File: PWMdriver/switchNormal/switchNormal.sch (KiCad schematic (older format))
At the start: 6 parts

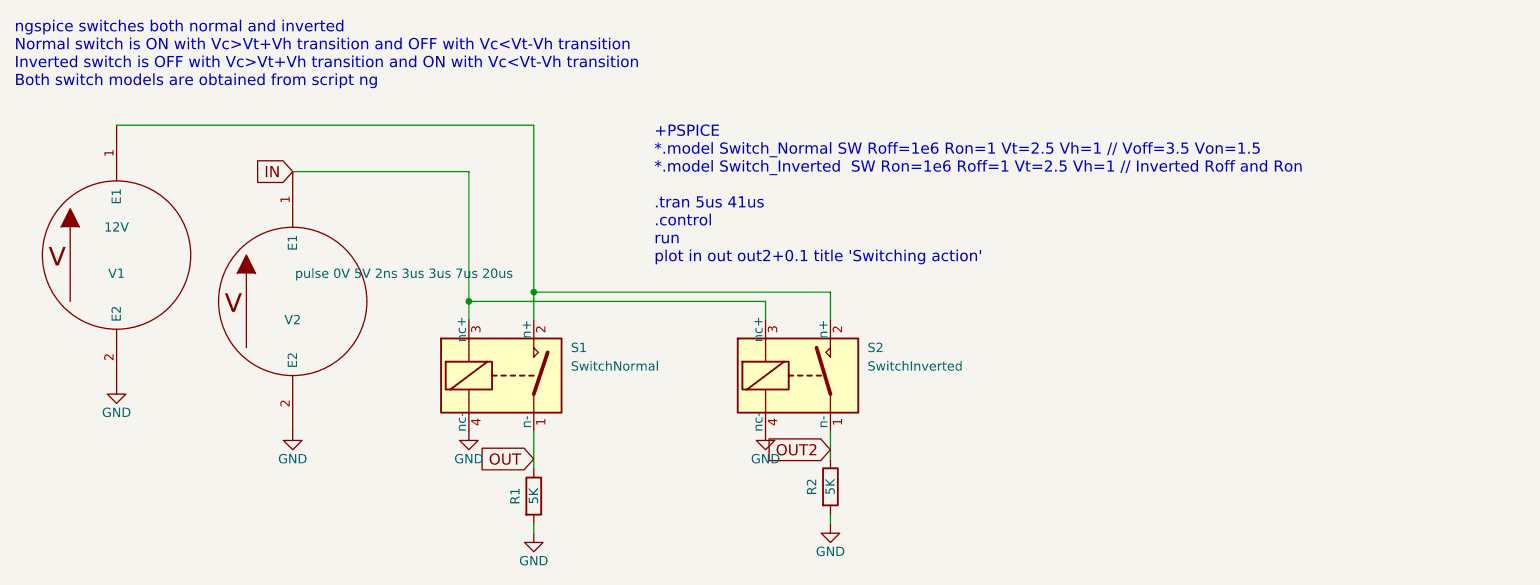
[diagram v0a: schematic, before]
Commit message: updated switches to NO and NC
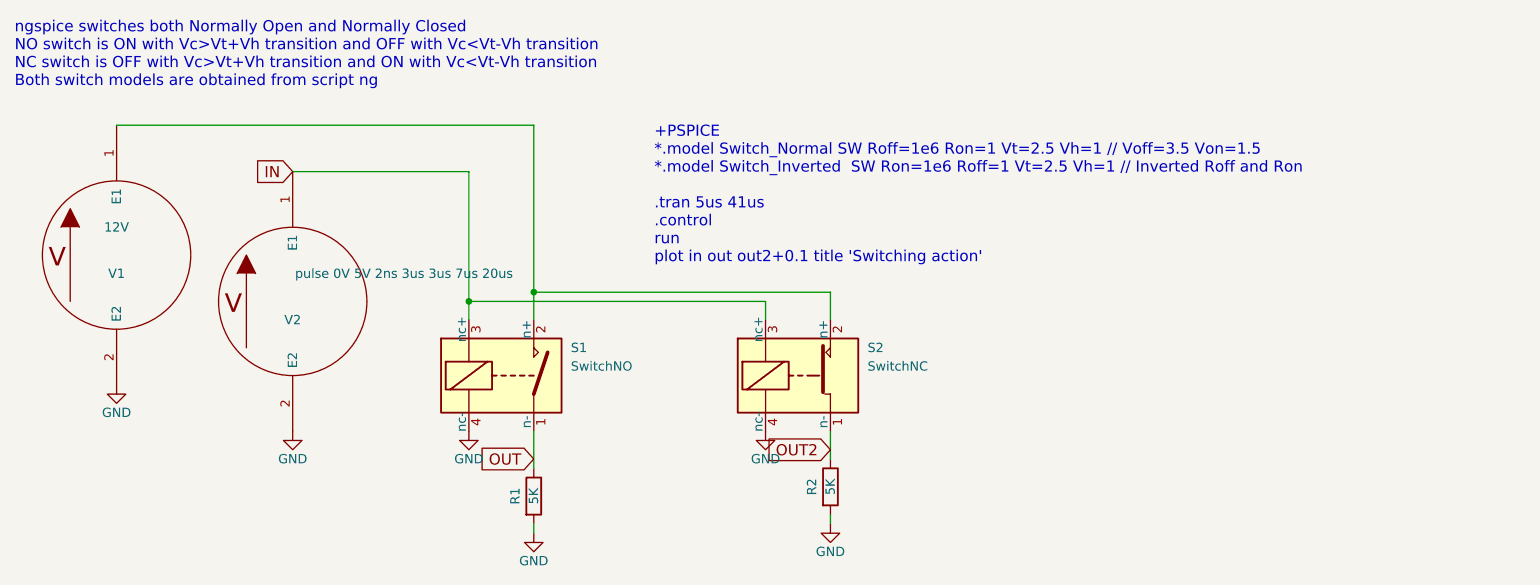
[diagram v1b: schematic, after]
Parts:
- removed S1: SwitchNormal, switchSpice, symbol SwitchNormal
- removed S2: SwitchInverted, switchSpice, symbol SwitchInverted
- added S1: SwitchNO, switchSpice, symbol SwitchNO
- added S2: SwitchNC, switchSpice, symbol SwitchNC
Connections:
- net GND: now also S1.4 (nc-), S2.4 (nc-)
- net IN: now also S1.3 (nc+), S2.3 (nc+)
- net OUT: now also S1.1 (n-)
- net OUT2: now also S2.1 (n-)
- net at V1.1 (E1): now also S1.2 (n+), S2.2 (n+)
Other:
- note added: "ngspice switches both Normally Open and Normally Closed\nNO switch is ON with Vc>Vt+Vh transition and OFF with Vc<Vt-Vh transition\nNC switch is OFF with Vc>Vt+Vh transition and ON with Vc<Vt-Vh transition\nBoth switch models are obtained from script ng"
- note removed: "ngspice switches both normal and inverted\nNormal switch is ON with Vc>Vt+Vh transition and OFF with Vc<Vt-Vh transition\nInverted switch is OFF with Vc>Vt+Vh transition and ON with Vc<Vt-Vh transition\nBoth switch models are obtained from script ng"
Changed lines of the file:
@@
 $EndDescr
 $Comp
-L GND #PWR01
+L GND #PWR3
 U 1 1 5B0C8932
 P 3650 2800
-F 0 "#PWR01" H 3650 2550 50  0001 C CNN
+F 0 "#PWR3" H 3650 2550 50  0001 C CNN
 F 1 "GND" H 3650 2650 50  0000 C CNN
 F 2 "" H 3650 2800 50  0001 C CNN
@@
 $EndComp
 $Comp
-L GND #PWR02
+L GND #PWR2
 U 1 1 5B0C8934
 P 2700 2800
-F 0 "#PWR02" H 2700 2550 50  0001 C CNN
+F 0 "#PWR2" H 2700 2550 50  0001 C CNN
 F 1 "GND" H 2700 2650 50  0000 C CNN
 F 2 "" H 2700 2800 50  0001 C CNN
@@
 	4000 3300 4000 3350
 $Comp
-L GND #PWR03
+L GND #PWR6
 U 1 1 5B0C8935
 P 4000 3350
-F 0 "#PWR03" H 4000 3100 50  0001 C CNN
+F 0 "#PWR6" H 4000 3100 50  0001 C CNN
 F 1 "GND" H 4000 3200 50  0000 C CNN
 F 2 "" H 4000 3350 50  0001 C CNN
@@
 $EndComp
 $Comp
-L GND #PWR04
+L GND #PWR1
 U 1 1 5B0C893B
 P 1750 2550
-F 0 "#PWR04" H 1750 2300 50  0001 C CNN
+F 0 "#PWR1" H 1750 2300 50  0001 C CNN
 F 1 "GND" H 1750 2400 50  0000 C CNN
 F 2 "" H 1750 2550 50  0001 C CNN
@@
 	4000 1150 1750 1150
 $Comp
-L GND #PWR05
+L GND #PWR4
 U 1 1 5B0D0161
 P 5250 2800
-F 0 "#PWR05" H 5250 2550 50  0001 C CNN
+F 0 "#PWR4" H 5250 2550 50  0001 C CNN
 F 1 "GND" H 5250 2650 50  0000 C CNN
 F 2 "" H 5250 2800 50  0001 C CNN
@@
 	5600 3250 5600 3300
 $Comp
-L GND #PWR06
+L GND #PWR5
 U 1 1 5B0D0169
 P 5600 3300
-F 0 "#PWR06" H 5600 3050 50  0001 C CNN
+F 0 "#PWR5" H 5600 3050 50  0001 C CNN
 F 1 "GND" H 5600 3150 50  0000 C CNN
 F 2 "" H 5600 3300 50  0001 C CNN
@@
 	5250 2100 3650 2100
 Text Notes 1200 950  0    60   ~ 0
-ngspice switches both normal and inverted\nNormal switch is ON with Vc>Vt+Vh transition and OFF with Vc<Vt-Vh transition\nInverted switch is OFF with Vc>Vt+Vh transition and ON with Vc<Vt-Vh transition\nBoth switch models are obtained from script ng
-$Comp
-L SwitchNormal S1
-U 1 1 5B0E5BFC
-P 3850 2500
-F 0 "S1" H 4200 2650 50  0000 L CNN
-F 1 "SwitchNormal" H 4200 2550 50  0000 L CNN
-F 2 "switchSpice" H 5120 2470 50  0001 C CNN
-F 3 "" H 3850 2500 50  0001 C CNN
-	1    3850 2500
-	1    0    0    -1
-$EndComp
-$Comp
-L SwitchInverted S2
-U 1 1 5B0E5CAD
-P 5450 2500
-F 0 "S2" H 5800 2650 50  0000 L CNN
-F 1 "SwitchInverted" H 5800 2550 50  0000 L CNN
-F 2 "switchSpice" H 6720 2470 50  0001 C CNN
-F 3 "" H 5450 2500 50  0001 C CNN
-	1    5450 2500
-	1    0    0    -1
-$EndComp
+ngspice switches both Normally Open and Normally Closed\nNO switch is ON with Vc>Vt+Vh transition and OFF with Vc<Vt-Vh transition\nNC switch is OFF with Vc>Vt+Vh transition and ON with Vc<Vt-Vh transition\nBoth switch models are obtained from script ng
 $Bitmap
 Pos 2700 5500
@@
 EndData
 $EndBitmap
+$Comp
+L SwitchNO S1
+U 1 1 5B14DEF0
+P 3850 2500
+F 0 "S1" H 4200 2650 50  0000 L CNN
+F 1 "SwitchNO" H 4200 2550 50  0000 L CNN
+F 2 "switchSpice" H 5120 2470 50  0001 C CNN
+F 3 "" H 3850 2500 50  0001 C CNN
+	1    3850 2500
+	1    0    0    -1
+$EndComp
+$Comp
+L SwitchNC S2
+U 1 1 5B14E355
+P 5450 2500
+F 0 "S2" H 5800 2650 50  0000 L CNN
+F 1 "SwitchNC" H 5800 2550 50  0000 L CNN
+F 2 "switchSpice" H 6720 2470 50  0001 C CNN
+F 3 "" H 5450 2500 50  0001 C CNN
+	1    5450 2500
+	1    0    0    -1
+$EndComp
 $EndSCHEMATC
